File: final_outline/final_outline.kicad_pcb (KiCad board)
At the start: 2 copper layers, 99.5 x 75 mm, 28 parts, among them P001 CANCONNECTOR, P002 AUXCONNECTOR, P100 ISP, P101 DEBUG_LED, U401 MCP2551-I/SN, U403 LPC11C14, U501 MCP1755-33, U502 MCP1755-5

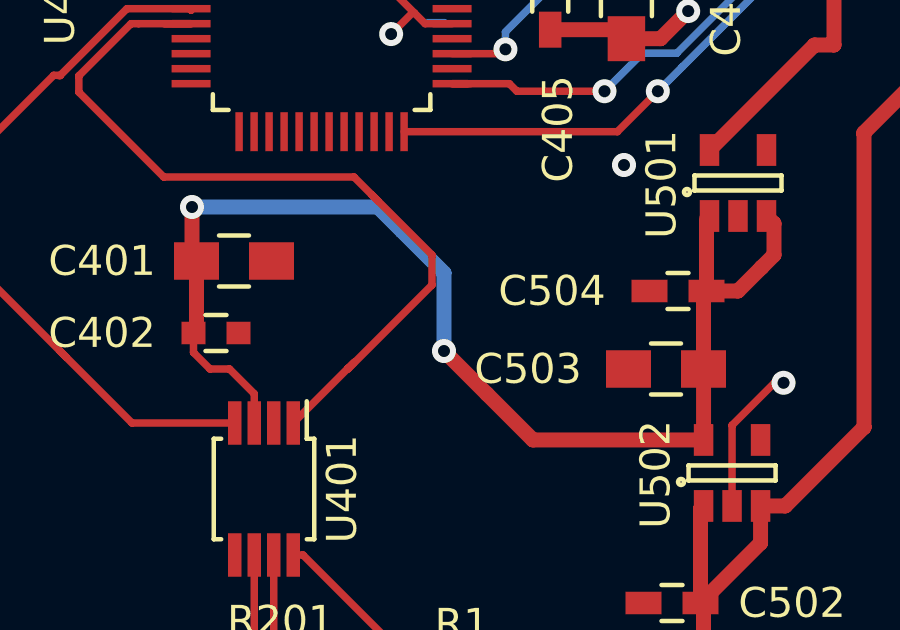
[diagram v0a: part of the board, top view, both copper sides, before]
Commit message: added ground plane via
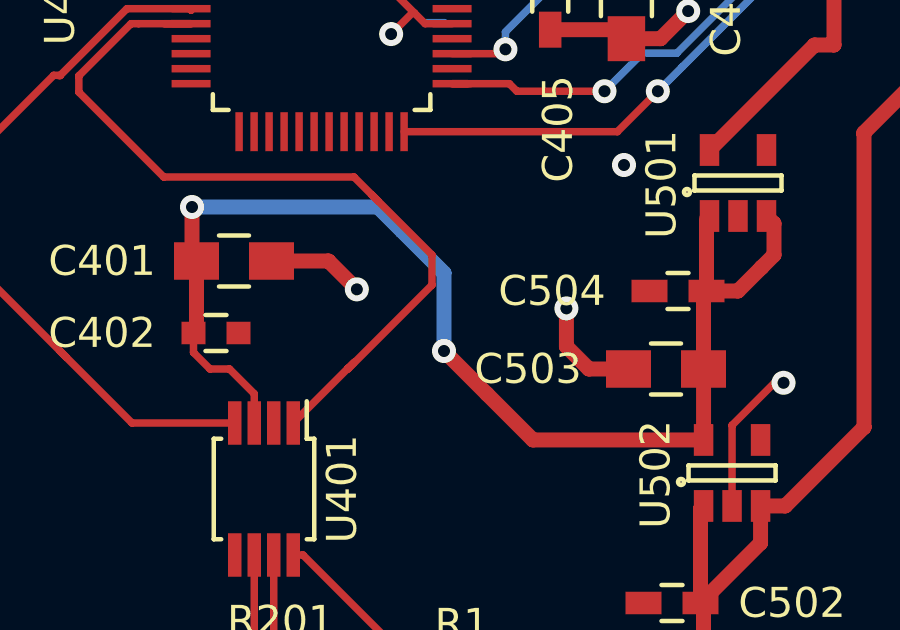
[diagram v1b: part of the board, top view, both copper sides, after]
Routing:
- net GND: track 22.2 -> 29.1 mm, vias 4 -> 6
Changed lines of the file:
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@@
     (thickness 1.6)
     (drawings 6)
-    (tracks 295)
+    (tracks 302)
     (zones 0)
     (modules 28)
@@
       (effects (font (size 1 1) (thickness 0.15)))
     )
-    (fp_text value 10μ (at -4.4 0 180) (layer F.Fab)
+    (fp_text value 10μ (at -4.2 0.8 180) (layer F.Fab)
       (effects (font (size 1 1) (thickness 0.15)))
     )
@@
   (segment (start 141.97 70.15) (end 141.97 70.3) (width 0.25) (layer F.Cu) (net 27))
   (segment (start 139 67.18) (end 141.97 70.15) (width 0.25) (layer F.Cu) (net 27))
+  (segment (start 122.25 92.4) (end 124.15 92.4) (width 0.5) (layer F.Cu) (net 28) (status 400000))
+  (via (at 125.095 93.345) (size 0.8) (drill 0.4) (layers F.Cu B.Cu) (net 28))
+  (segment (start 124.15 92.4) (end 125.095 93.345) (width 0.5) (layer F.Cu) (net 28))
+  (segment (start 134.15 96) (end 132.83 96) (width 0.5) (layer F.Cu) (net 28))
+  (via (at 132.08 93.98) (size 0.8) (drill 0.4) (layers F.Cu B.Cu) (net 28))
+  (segment (start 132.08 95.25) (end 132.08 93.98) (width 0.5) (layer F.Cu) (net 28))
+  (segment (start 132.83 96) (end 132.08 95.25) (width 0.5) (layer F.Cu) (net 28))
   (segment (start 137.602 100.565) (end 137.602 97.874998) (width 0.25) (layer F.Cu) (net 28))
   (segment (start 137.602 97.874998) (end 139.016998 96.46) (width 0.25) (layer F.Cu) (net 28))

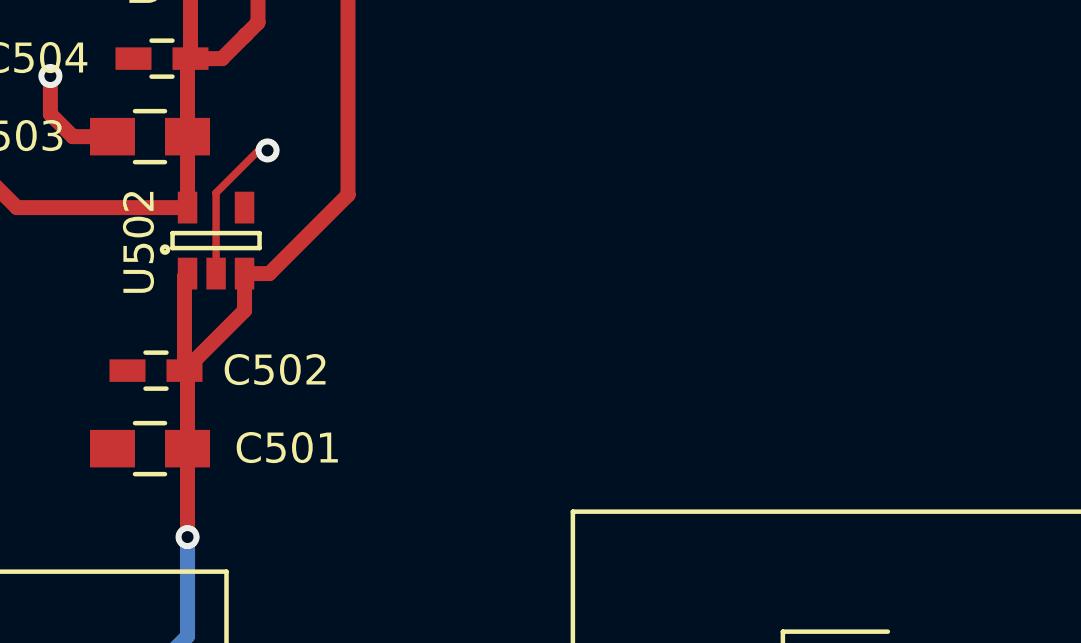
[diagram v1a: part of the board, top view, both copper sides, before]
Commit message: some last updates for the template, added 10V regulator
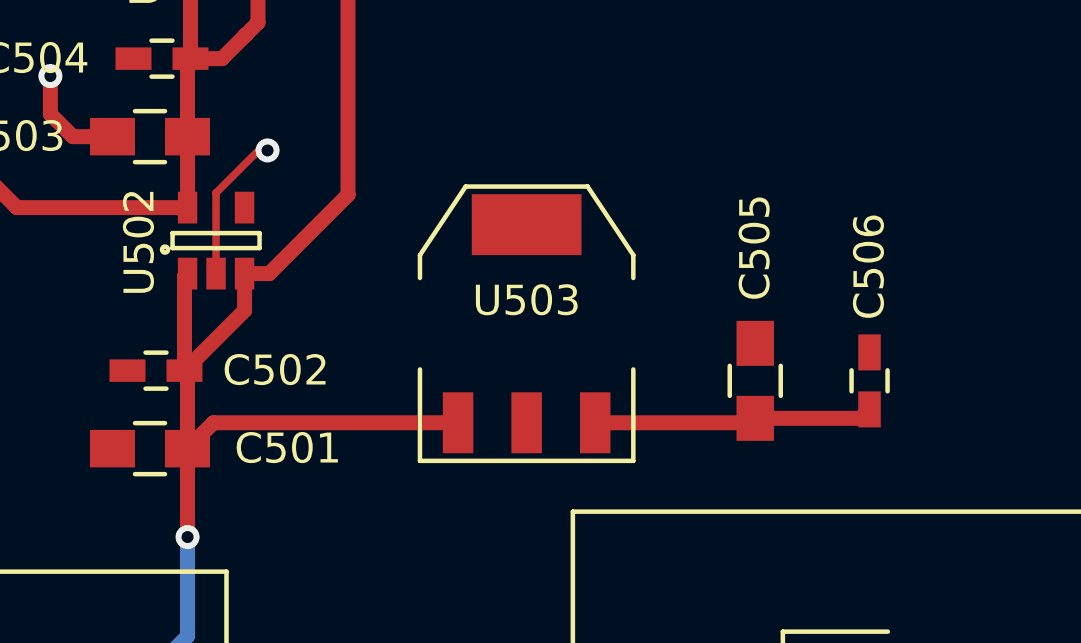
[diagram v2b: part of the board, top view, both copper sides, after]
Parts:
- added C505: 10μ, Capacitors_SMD:C_0805_HandSoldering, F.Cu at (155.6, 104.1)
- added C506: .1μ, Capacitors_SMD:C_0603_HandSoldering, F.Cu at (159.4, 104.1)
- added U503: Zsr1000gta, TO_SOT_Packages_SMD:SOT-223, F.Cu at (148.0, 102.2)
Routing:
- net +12V: track 113.5 -> 122.9 mm
- net VCC: track 0.00 -> 9.33 mm

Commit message: When I tried to close it, I got a message requesting me to save...
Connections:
- P100 pad 3: +12V -> +5V
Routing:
- net +12V: track 122.9 -> 42.1 mm
- net +5V: track 41.8 -> 113.2 mm
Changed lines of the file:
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@@
       (net 32 /FRONT_PANEL/MCU_PROG_N))
     (pad 3 thru_hole circle (at -6 0 180) (size 1.5 1.5) (drill 1.1) (layers *.Cu *.Mask F.SilkS)
-      (net 82 +12V))
+      (net 77 +5V))
     (pad "" np_thru_hole circle (at -3 4.32 180) (size 3.1 3.1) (drill 3.1) (layers *.Cu *.Mask F.SilkS))
   )
@@
   (segment (start 136 68) (end 137 69) (width 0.25) (layer F.Cu) (net 76))
   (segment (start 136 65) (end 136 68) (width 0.25) (layer F.Cu) (net 76))
+  (segment (start 142 88.6) (end 142 88.8) (width 0.5) (layer F.Cu) (net 77))
+  (segment (start 142 88.124) (end 141.986 88.138) (width 0.25) (layer F.Cu) (net 77))
+  (segment (start 158.242 68.834) (end 185.801 68.834) (width 0.5) (layer F.Cu) (net 77))
+  (segment (start 153.289 73.787) (end 158.242 68.834) (width 0.5) (layer F.Cu) (net 77))
+  (segment (start 153.289 83.566) (end 153.289 73.787) (width 0.5) (layer F.Cu) (net 77))
+  (segment (start 151.003 85.852) (end 153.289 83.566) (width 0.5) (layer F.Cu) (net 77))
+  (segment (start 144.272 85.852) (end 151.003 85.852) (width 0.5) (layer F.Cu) (net 77))
+  (segment (start 141.986 88.138) (end 144.272 85.852) (width 0.5) (layer F.Cu) (net 77))
+  (segment (start 142 88.124) (end 142 88.6) (width 0.5) (layer F.Cu) (net 77))
+  (segment (start 188.595 66.04) (end 188.595 64.965) (width 0.5) (layer F.Cu) (net 77))
+  (segment (start 185.88 62.25) (end 188.595 64.965) (width 0.5) (layer F.Cu) (net 77))
+  (segment (start 185.801 68.834) (end 188.595 66.04) (width 0.5) (layer F.Cu) (net 77))
+  (segment (start 142 88.8) (end 139 91.8) (width 0.5) (layer F.Cu) (net 77))
   (segment (start 136.75 93.4) (end 136.75 91) (width 0.5) (layer F.Cu) (net 77))
   (segment (start 136.75 93.4) (end 137.8 93.4) (width 0.5) (layer F.Cu) (net 77))
@@
   (segment (start 136.652 96.002) (end 136.65 96) (width 0.5) (layer F.Cu) (net 77))
   (segment (start 138.6 92.6) (end 139 92.2) (width 0.5) (layer F.Cu) (net 77))
-  (segment (start 139 92.2) (end 139 91.15) (width 0.5) (layer F.Cu) (net 77))
+  (segment (start 139 92.2) (end 139 91.8) (width 0.5) (layer F.Cu) (net 77))
+  (segment (start 139 91.8) (end 139 91.15) (width 0.5) (layer F.Cu) (net 77))
   (segment (start 139 91.15) (end 138.75 90.9) (width 0.5) (layer F.Cu) (net 77))
   (segment (start 136.652 98.365) (end 130.965 98.365) (width 0.5) (layer F.Cu) (net 77))
@@
   (segment (start 136.652 108.781315) (end 136.65 108.779315) (width 0.5) (layer F.Cu) (net 82))
   (segment (start 136.65 108.779315) (end 136.65 106.4) (width 0.5) (layer F.Cu) (net 82))
-  (segment (start 142 88.124) (end 142 97.942) (width 0.5) (layer F.Cu) (net 82))
-  (segment (start 141.986 88.138) (end 144.272 85.852) (width 0.5) (layer F.Cu) (net 82))
-  (segment (start 144.272 85.852) (end 151.003 85.852) (width 0.5) (layer F.Cu) (net 82))
-  (segment (start 151.003 85.852) (end 153.289 83.566) (width 0.5) (layer F.Cu) (net 82))
-  (segment (start 153.289 83.566) (end 153.289 73.787) (width 0.5) (layer F.Cu) (net 82))
-  (segment (start 153.289 73.787) (end 158.242 68.834) (width 0.5) (layer F.Cu) (net 82))
-  (segment (start 158.242 68.834) (end 185.801 68.834) (width 0.5) (layer F.Cu) (net 82))
-  (segment (start 185.801 68.834) (end 188.595 66.04) (width 0.5) (layer F.Cu) (net 82))
-  (segment (start 188.595 64.965) (end 185.88 62.25) (width 0.5) (layer F.Cu) (net 82))
-  (segment (start 188.595 66.04) (end 188.595 64.965) (width 0.5) (layer F.Cu) (net 82))
-  (segment (start 142 88.124) (end 141.986 88.138) (width 0.25) (layer F.Cu) (net 82))
   (segment (start 128.87132 118.5) (end 128.88032 118.491) (width 0.5) (layer B.Cu) (net 82))
   (segment (start 128.87132 118.5) (end 126.75 118.5) (width 0.5) (layer B.Cu) (net 82))
@@
   (segment (start 130.81 118.491) (end 136.652 112.649) (width 0.5) (layer B.Cu) (net 82))
   (segment (start 136.652 109.347) (end 136.652 108.781315) (width 0.5) (layer F.Cu) (net 82))
-  (segment (start 138.552 100.565) (end 139.377 100.565) (width 0.5) (layer F.Cu) (net 82))
-  (segment (start 139.377 100.565) (end 142 97.942) (width 0.5) (layer F.Cu) (net 82))
-  (segment (start 142 97.942) (end 141.986 97.956) (width 0.5) (layer F.Cu) (net 82))
   (segment (start 122.75 118.5) (end 126.75 118.5) (width 0.5) (layer F.Cu) (net 82))
   (segment (start 122.975 102.2) (end 123.3 102.2) (width 0.25) (layer F.Cu) (net 84))

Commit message: Fixed pins
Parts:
- C402: footprint Capacitors_SMD:C_0603 -> Capacitors_SMD:C_0603_HandSoldering
- P002: value AUXCONNECTOR -> CONN_01X14; footprint MITEVT_AUTOMOTIVECON:776087-1 -> MITEVT_AUTOMOTIVECON:776267-1
- moved P002 4.07 mm to (162.6, 114.3)
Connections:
- P002 pad 15: Net-(P002-Pad15) -> (no net)
- P002 pad 16: Net-(P002-Pad16) -> (no net)
